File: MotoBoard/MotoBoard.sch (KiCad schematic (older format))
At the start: 13 parts, among them U1 ATmega2560-16AU

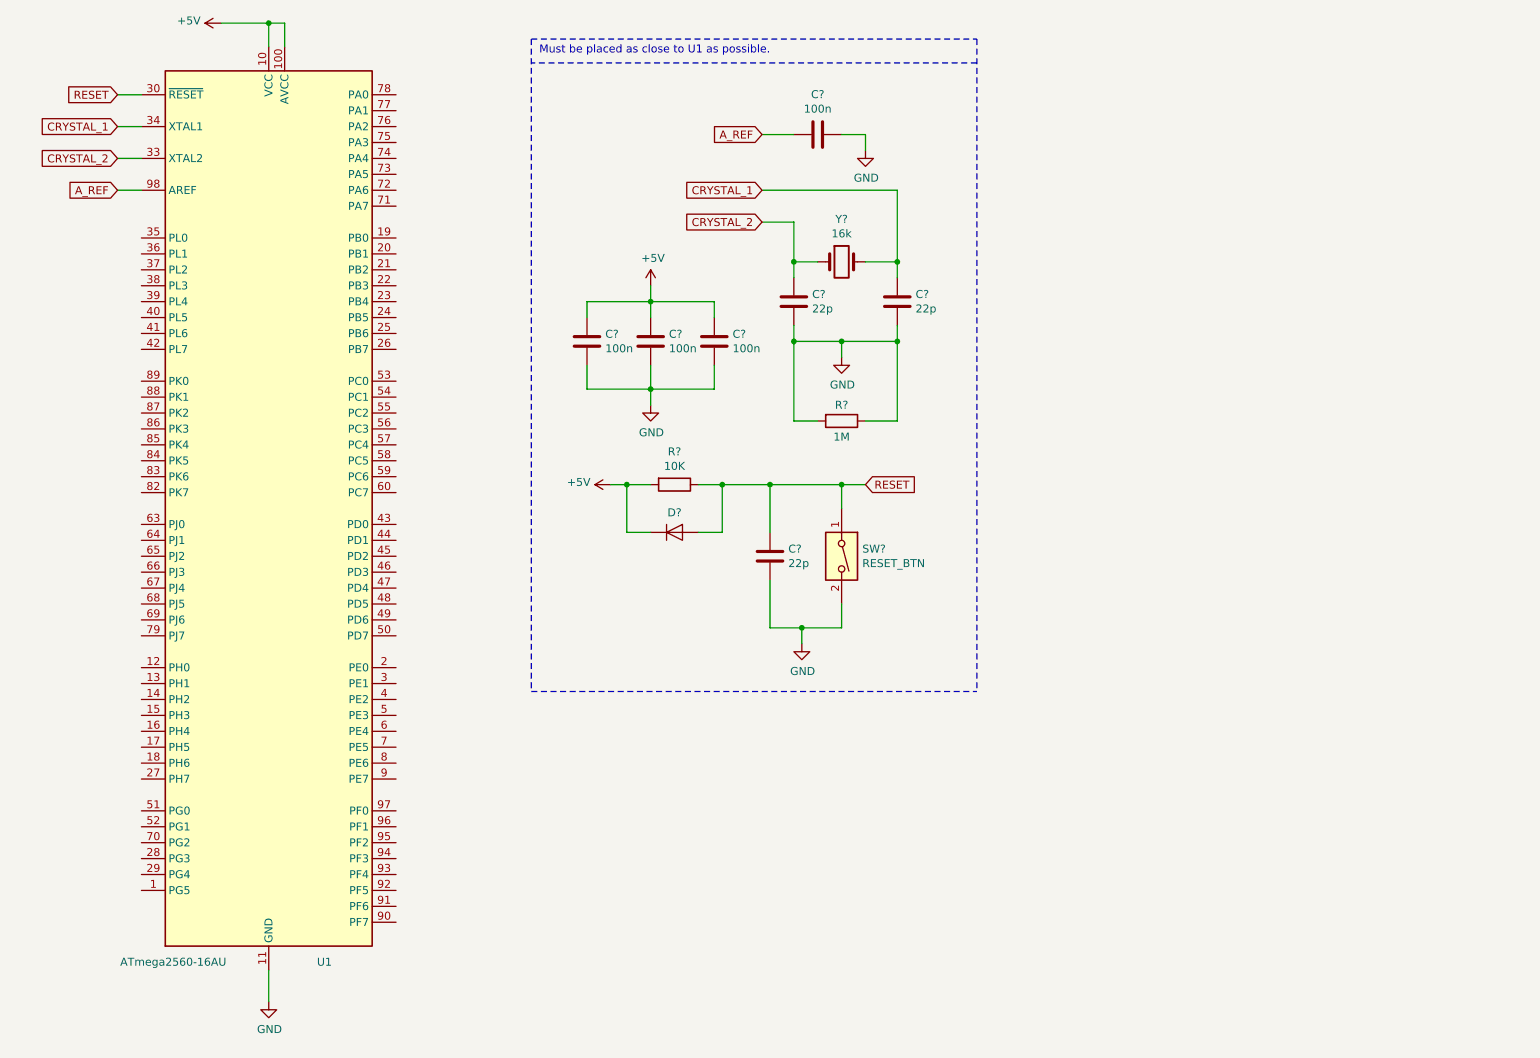
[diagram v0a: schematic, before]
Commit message: Added all connections to main MCU
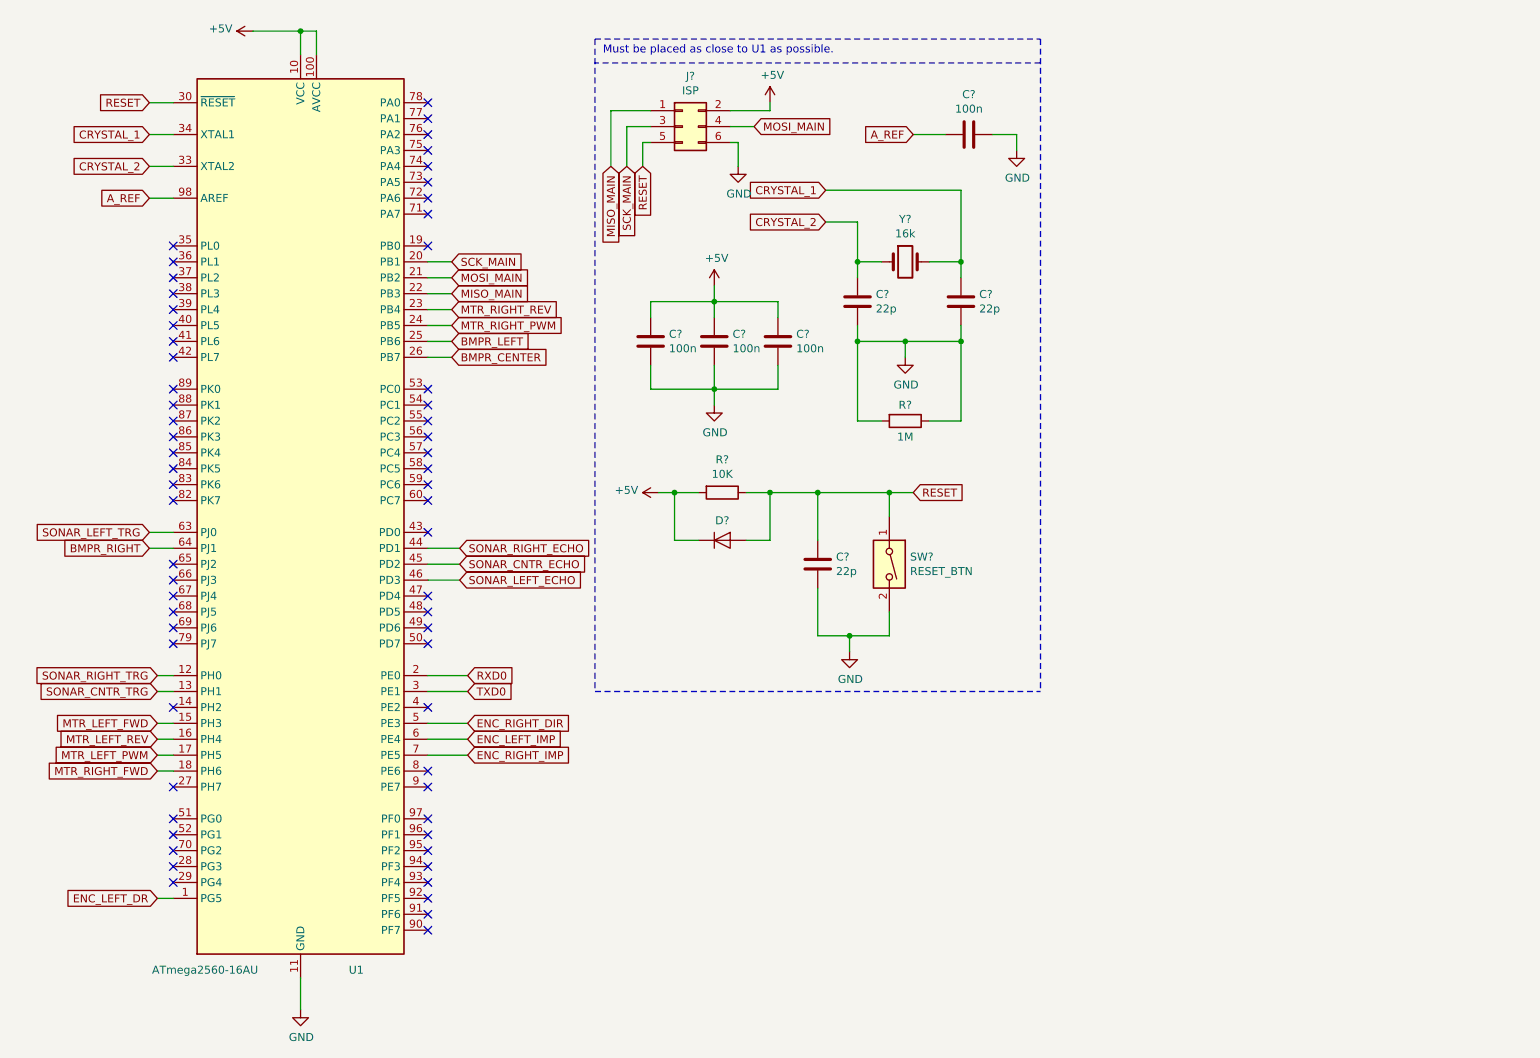
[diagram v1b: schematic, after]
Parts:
- added J?: ISP, symbol Connector_Generic:Conn_02x03_Odd_Even
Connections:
- net +5V: now also J?.2 (Pin_2)
- net GND: now also J?.6 (Pin_6)
- net RESET: now also J?.5 (Pin_5)
- net ENC_LEFT_DR: now reaches U1.1 (PG5)
- net SONAR_RIGHT_TRG: now reaches U1.12 (PH0)
- net SONAR_CNTR_TRG: now reaches U1.13 (PH1)
- net MTR_LEFT_FWD: now reaches U1.15 (PH3)
- net MTR_LEFT_REV: now reaches U1.16 (PH4)
- net MTR_LEFT_PWM: now reaches U1.17 (PH5)
- net MTR_RIGHT_FWD: now reaches U1.18 (PH6)
- net RXD0: now reaches U1.2 (PE0)
- net SCK_MAIN: now reaches U1.20 (PB1)
- net SCK_MAIN: now also J?.3 (Pin_3)
- net MOSI_MAIN: now reaches U1.21 (PB2)
- net MOSI_MAIN: now also J?.4 (Pin_4)
- net MISO_MAIN: now reaches U1.22 (PB3)
- net MISO_MAIN: now also J?.1 (Pin_1)
- net MTR_RIGHT_REV: now reaches U1.23 (PB4)
- net MTR_RIGHT_PWM: now reaches U1.24 (PB5)
- net BMPR_LEFT: now reaches U1.25 (PB6)
- net BMPR_CENTER: now reaches U1.26 (PB7)
- net TXD0: now reaches U1.3 (PE1)
- net SONAR_RIGHT_ECHO: now reaches U1.44 (PD1)
- net SONAR_CNTR_ECHO: now reaches U1.45 (PD2)
- net SONAR_LEFT_ECHO: now reaches U1.46 (PD3)
- net ENC_RIGHT_DIR: now reaches U1.5 (PE3)
- net ENC_LEFT_IMP: now reaches U1.6 (PE4)
- net SONAR_LEFT_TRG: now reaches U1.63 (PJ0)
- net BMPR_RIGHT: now reaches U1.64 (PJ1)
- net ENC_RIGHT_IMP: now reaches U1.7 (PE5)
- no-connect marks 0 -> 62
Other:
- moved on the sheet: C?, D?, R?, SW?, U1, Y?

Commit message: More work on moto board
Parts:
- added J?: USB_B, symbol Connector:USB_B
- added R? (x2): 22R, Resistor_SMD:R_1206_3216Metric, symbol Device:R
- added U?: ATmega16U2-AU, Package_QFP:TQFP-32_7x7mm_P0.8mm, symbol MCU_Microchip_ATmega:ATmega16U2-AU
- J?: footprint (none) -> Connector_PinHeader_1.00mm:PinHeader_2x03_P1.00mm_Vertical
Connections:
- new net: R?.1, U?.29 (D+)
- new net: R?.1, U?.30 (D-)
- new net: J?.2 (D-), R?.2
- new net: J?.3 (D+), R?.2
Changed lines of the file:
@@
 F 0 "J?" H 4650 1617 50  0000 C CNN
 F 1 "ISP" H 4650 1526 50  0000 C CNN
-F 2 "" H 4600 1300 50  0001 C CNN
+F 2 "Connector_PinHeader_1.00mm:PinHeader_2x03_P1.00mm_Vertical" H 4600 1300 50  0001 C CNN
 F 3 "~" H 4600 1300 50  0001 C CNN
 	1    4600 1300
@@
 NoConn ~ 3000 1250
 NoConn ~ 3000 1150
+$Comp
+L MCU_Microchip_ATmega:ATmega16U2-AU U?
+U 1 1 5FDFCC29
+P 9200 2450
+F 0 "U?" H 9200 961 50  0000 C CNN
+F 1 "ATmega16U2-AU" H 9200 870 50  0000 C CNN
+F 2 "Package_QFP:TQFP-32_7x7mm_P0.8mm" H 9200 2450 50  0001 C CIN
+F 3 "http://ww1.microchip.com/downloads/en/DeviceDoc/doc7799.pdf" H 9200 2450 50  0001 C CNN
+	1    9200 2450
+	1    0    0    -1
+$EndComp
+$Comp
+L Connector:USB_B J?
+U 1 1 5FE000CF
+P 7350 1950
+F 0 "J?" H 7407 2417 50  0000 C CNN
+F 1 "USB_B" H 7407 2326 50  0000 C CNN
+F 2 "" H 7500 1900 50  0001 C CNN
+F 3 " ~" H 7500 1900 50  0001 C CNN
+	1    7350 1950
+	1    0    0    -1
+$EndComp
+$Comp
+L Device:R R?
+U 1 1 5FE00E61
+P 8100 1950
+F 0 "R?" V 7893 1950 50  0000 C CNN
+F 1 "22R" V 7984 1950 50  0000 C CNN
+F 2 "Resistor_SMD:R_1206_3216Metric" V 8030 1950 50  0001 C CNN
+F 3 "~" H 8100 1950 50  0001 C CNN
+	1    8100 1950
+	0    1    1    0
+$EndComp
+$Comp
+L Device:R R?
+U 1 1 5FE016D7
+P 8100 2050
+F 0 "R?" V 8200 2050 50  0000 C CNN
+F 1 "22R" V 8300 2050 50  0000 C CNN
+F 2 "Resistor_SMD:R_1206_3216Metric" V 8030 2050 50  0001 C CNN
+F 3 "~" H 8100 2050 50  0001 C CNN
+	1    8100 2050
+	0    1    1    0
+$EndComp
+Wire Wire Line
+	8250 2050 8500 2050
+Wire Wire Line
+	8250 1950 8500 1950
+Wire Wire Line
+	7950 1950 7650 1950
+Wire Wire Line
+	7650 2050 7950 2050
+$Comp
+L power:GND #PWR?
+U 1 1 5FE1B4B1
+P 7650 2850
+F 0 "#PWR?" H 7650 2600 50  0001 C CNN
+F 1 "GND" H 7655 2677 50  0000 C CNN
+F 2 "" H 7650 2850 50  0001 C CNN
+F 3 "" H 7650 2850 50  0001 C CNN
+	1    7650 2850
+	1    0    0    -1
+$EndComp
 $EndSCHEMATC
